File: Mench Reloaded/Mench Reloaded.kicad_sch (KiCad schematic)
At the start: 41 parts, among them IC1 DS1813, J2 Barrel_Jack_Switch, SW1 SW_Push, U1 W65C265SxQ, U5 LM7805_TO220, Y1 32.768 kHz, Y2 3.6864 mHz

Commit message: First draft of PCB
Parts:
- removed C10: 0.1uF, symbol Device:C_Small
- removed C11: 10uF, symbol Device:C_Polarized_US
- removed C9: 0.33uF, symbol Device:C_Small
- removed D1: LED, symbol Device:LED
- removed J2: Barrel_Jack_Switch, symbol Connector:Barrel_Jack_Switch
- removed R1: R_US, symbol Device:R_US
- removed U5: LM7805_TO220, Package_TO_SOT_THT:TO-220-3_Vertical, symbol Regulator_Linear:LM7805_TO220
- C1: renamed from C6; footprint (none) -> Capacitor_SMD:C_0805_2012Metric_Pad1.18x1.45mm_HandSolder
- C2: renamed from C8; footprint (none) -> Capacitor_SMD:C_0805_2012Metric_Pad1.18x1.45mm_HandSolder
- C3: renamed from C5; footprint (none) -> Capacitor_SMD:C_0805_2012Metric_Pad1.18x1.45mm_HandSolder
- C4: renamed from C7; footprint (none) -> Capacitor_SMD:C_0805_2012Metric_Pad1.18x1.45mm_HandSolder
- C5: renamed from C1; footprint (none) -> Capacitor_SMD:C_0805_2012Metric_Pad1.18x1.45mm_HandSolder
- C6: renamed from C2; footprint (none) -> Capacitor_SMD:C_0805_2012Metric_Pad1.18x1.45mm_HandSolder
- C7: renamed from C3; footprint (none) -> Capacitor_SMD:C_0805_2012Metric_Pad1.18x1.45mm_HandSolder
- C8: renamed from C4; footprint (none) -> Capacitor_SMD:C_0805_2012Metric_Pad1.18x1.45mm_HandSolder
- D1, D2, D3, D4, D5, D6, D7, D8: footprint (none) -> LED_SMD:LED_0805_2012Metric_Pad1.15x1.40mm_HandSolder
- IC1: footprint ds1813_revised-TO-92 -> ds1813_revised:ds1813_revised-TO-92
- R1: renamed from R4; footprint (none) -> Resistor_SMD:R_0805_2012Metric_Pad1.20x1.40mm_HandSolder
- R10: renamed from R11; footprint (none) -> Resistor_SMD:R_0805_2012Metric_Pad1.20x1.40mm_HandSolder
- R11: renamed from R12; footprint (none) -> Resistor_SMD:R_0805_2012Metric_Pad1.20x1.40mm_HandSolder
- R12: renamed from R13; footprint (none) -> Resistor_SMD:R_0805_2012Metric_Pad1.20x1.40mm_HandSolder
- R2: footprint (none) -> Resistor_SMD:R_0805_2012Metric_Pad1.20x1.40mm_HandSolder
- R3: renamed from R5; footprint (none) -> Resistor_SMD:R_0805_2012Metric_Pad1.20x1.40mm_HandSolder
- R4: renamed from R3; footprint (none) -> Resistor_SMD:R_0805_2012Metric_Pad1.20x1.40mm_HandSolder
- R5: renamed from R6; footprint (none) -> Resistor_SMD:R_0805_2012Metric_Pad1.20x1.40mm_HandSolder
- R6: renamed from R7; footprint (none) -> Resistor_SMD:R_0805_2012Metric_Pad1.20x1.40mm_HandSolder
- R7: renamed from R8; footprint (none) -> Resistor_SMD:R_0805_2012Metric_Pad1.20x1.40mm_HandSolder
- R8: renamed from R9; footprint (none) -> Resistor_SMD:R_0805_2012Metric_Pad1.20x1.40mm_HandSolder
- R9: renamed from R10; footprint (none) -> Resistor_SMD:R_0805_2012Metric_Pad1.20x1.40mm_HandSolder
- SW1: footprint (none) -> Button_Switch_THT:SW_PUSH_6mm_H5mm
- Y1: footprint (none) -> Crystal:Crystal_C26-LF_D2.1mm_L6.5mm_Horizontal
- Y2: footprint (none) -> Crystal:Crystal_HC49-U_Vertical
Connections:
- net BA: now reaches U1.39 (BA/~{DOD})
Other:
- moved on the sheet: C5, C6, C7, C8, D1, D2, D3, D4, D5, D6, D7, D8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

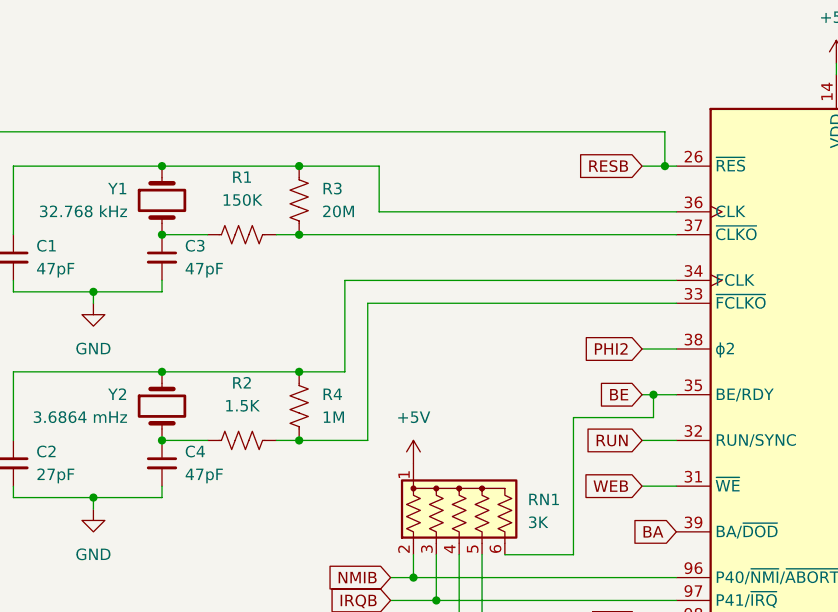
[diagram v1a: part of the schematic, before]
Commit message: Completed initial PCB layout. Commiting because I will try to reduce it to 100mm x 100mm
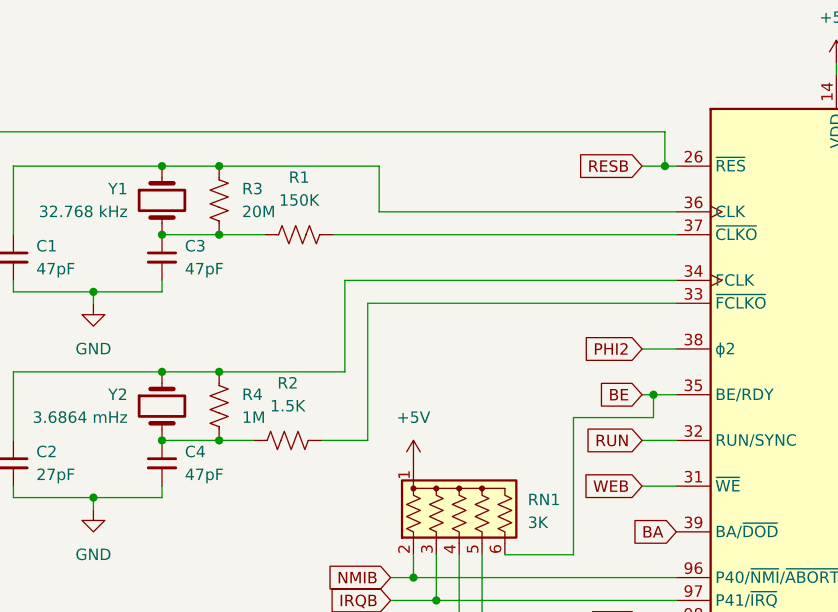
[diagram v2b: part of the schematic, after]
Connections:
- net at R2.2, U1.33 (~{FCLKO}): no longer R4.1
- net at R1.2, U1.37 (~{CLKO}): no longer R3.1
- net at C3.1, R1.1, Y1.2: now also R3.1
- net at C4.1, R2.1, Y2.2: now also R4.1
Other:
- moved on the sheet: R1, R2

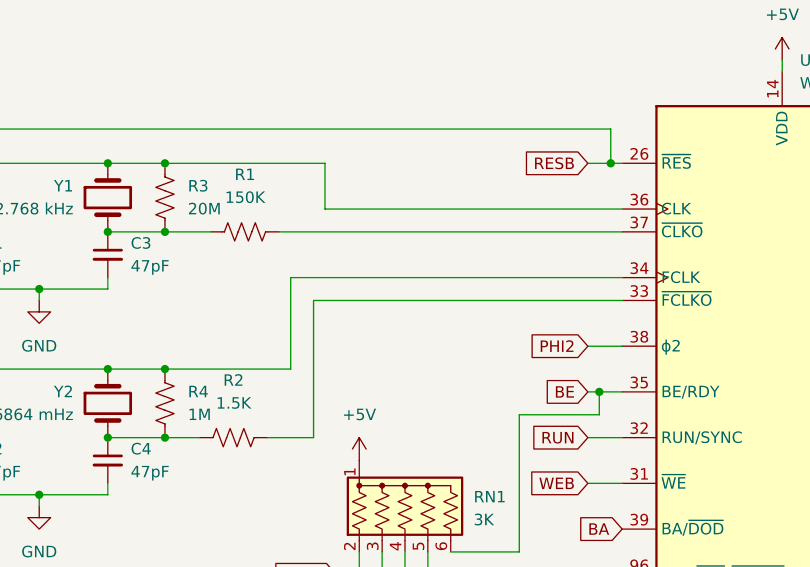
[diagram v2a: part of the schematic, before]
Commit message: Reworked the layout to 100mm by 100mm. Also changed the headers to be compatible with the W65C265SXB.
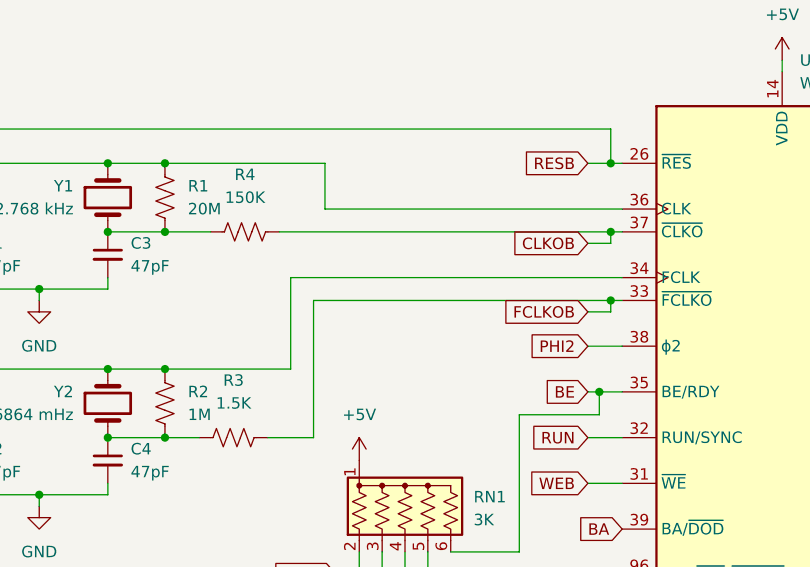
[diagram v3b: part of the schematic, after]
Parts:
- renumbered R3 to R1, R4 to R2, R2 to R3, R1 to R4
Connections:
- net FCLKOB: now reaches R3.2, U1.33 (~{FCLKO})
- net CLKOB: now reaches R4.2, U1.37 (~{CLKO})
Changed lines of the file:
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@@
   (junction (at 80.01 60.96) (diameter 0) (color 0 0 0 0)
   )
+  (junction (at 129.54 38.1) (diameter 0) (color 0 0 0 0)
+  )
   (junction (at 271.78 107.95) (diameter 0) (color 0 0 0 0)
   )
@@
   (junction (at 109.22 86.36) (diameter 0) (color 0 0 0 0)
   )
+  (junction (at 129.54 45.72) (diameter 0) (color 0 0 0 0)
+  )
   (junction (at 254 31.75) (diameter 0) (color 0 0 0 0)
   )
@@
     (stroke (width 0) (type default))
   )
-  (wire (pts (xy 96.52 45.72) (xy 130.81 45.72))
+  (wire (pts (xy 96.52 45.72) (xy 129.54 45.72))
     (stroke (width 0) (type default))
   )
@@
     (stroke (width 0) (type default))
   )
+  (wire (pts (xy 129.54 45.72) (xy 130.81 45.72))
+    (stroke (width 0) (type default))
+  )
   (bus (pts (xy 185.42 76.2) (xy 185.42 73.66))
     (stroke (width 0) (type default))
@@
     (stroke (width 0) (type default))
   )
+  (wire (pts (xy 129.54 38.1) (xy 129.54 39.37))
+    (stroke (width 0) (type default))
+  )
   (bus (pts (xy 185.42 121.92) (xy 185.42 119.38))
     (stroke (width 0) (type default))
@@
     (stroke (width 0) (type default))
   )
+  (wire (pts (xy 129.54 38.1) (xy 130.81 38.1))
+    (stroke (width 0) (type default))
+  )
   (wire (pts (xy 129.54 30.48) (xy 130.81 30.48))
     (stroke (width 0) (type default))
@@
     (stroke (width 0) (type default))
   )
+  (wire (pts (xy 127 46.99) (xy 129.54 46.99))
+    (stroke (width 0) (type default))
+  )
   (wire (pts (xy 129.54 26.67) (xy 44.45 26.67))
     (stroke (width 0) (type default))
@@
     (stroke (width 0) (type default))
   )
-  (wire (pts (xy 92.71 38.1) (xy 130.81 38.1))
+  (wire (pts (xy 92.71 38.1) (xy 129.54 38.1))
     (stroke (width 0) (type default))
   )
@@
     (stroke (width 0) (type default))
   )
+  (wire (pts (xy 129.54 46.99) (xy 129.54 45.72))
+    (stroke (width 0) (type default))
+  )
   (wire (pts (xy 271.78 87.63) (xy 271.78 97.79))
     (stroke (width 0) (type default))
@@
   )
   (wire (pts (xy 148.59 19.05) (xy 148.59 20.32))
+    (stroke (width 0) (type default))
+  )
+  (wire (pts (xy 129.54 39.37) (xy 127 39.37))
     (stroke (width 0) (type default))
   )
@@
     )
   )
+  (global_label "FCLKOB" (shape input) (at 127 46.99 180) (fields_autoplaced)
+    (effects (font (size 1.27 1.27)) (justify right))
+    (property "Intersheetrefs" "${INTERSHEET_REFS}" (at 116.7419 46.99 0)
+      (effects (font (size 1.27 1.27)) (justify right) hide)
+    )
+  )
   (global_label "csb[0..7]" (shape input) (at 242.57 83.82 180) (fields_autoplaced)
     (effects (font (size 1.27 1.27)) (justify right))
@@
     (effects (font (size 1.27 1.27)) (justify right))
     (property "Intersheetrefs" "${INTERSHEET_REFS}" (at 91.4629 83.82 0)
+      (effects (font (size 1.27 1.27)) (justify right) hide)
+    )
+  )
+  (global_label "CLKOB" (shape input) (at 127 39.37 180) (fields_autoplaced)
+    (effects (font (size 1.27 1.27)) (justify right))
+    (property "Intersheetrefs" "${INTERSHEET_REFS}" (at 117.8305 39.37 0)
       (effects (font (size 1.27 1.27)) (justify right) hide)
     )
@@
   (symbol (lib_id "Device:R_US") (at 80.01 34.29 180) (unit 1)
     (in_bom yes) (on_board yes) (dnp no) (fields_autoplaced)
-    (property "Reference" "R3" (at 82.55 33.02 0)
+    (property "Reference" "R1" (at 82.55 33.02 0)
       (effects (font (size 1.27 1.27)) (justify right))
     )
@@
       (project "Mench Reloaded"
         (path "/e63e39d7-6ac0-4ffd-8aa3-1841a4541b55"
-          (reference "R3") (unit 1)
+          (reference "R1") (unit 1)
         )
       )
@@
   (symbol (lib_id "Device:R_US") (at 88.9 38.1 90) (unit 1)
     (in_bom yes) (on_board yes) (dnp no) (fields_autoplaced)
-    (property "Reference" "R1" (at 88.9 31.75 90)
+    (property "Reference" "R4" (at 88.9 31.75 90)
       (effects (font (size 1.27 1.27)))
     )
@@
       (project "Mench Reloaded"
         (path "/e63e39d7-6ac0-4ffd-8aa3-1841a4541b55"
-          (reference "R1") (unit 1)
+          (reference "R4") (unit 1)
         )
       )
@@
   (symbol (lib_id "Device:R_US") (at 87.63 60.96 90) (unit 1)
     (in_bom yes) (on_board yes) (dnp no) (fields_autoplaced)
-    (property "Reference" "R2" (at 87.63 54.61 90)
+    (property "Reference" "R3" (at 87.63 54.61 90)
       (effects (font (size 1.27 1.27)))
     )
@@
       (project "Mench Reloaded"
         (path "/e63e39d7-6ac0-4ffd-8aa3-1841a4541b55"
-          (reference "R2") (unit 1)
+          (reference "R3") (unit 1)
         )
       )
@@
   (symbol (lib_id "Device:R_US") (at 80.01 57.15 180) (unit 1)
     (in_bom yes) (on_board yes) (dnp no) (fields_autoplaced)
-    (property "Reference" "R4" (at 82.55 55.88 0)
+    (property "Reference" "R2" (at 82.55 55.88 0)
       (effects (font (size 1.27 1.27)) (justify right))
     )
@@
       (project "Mench Reloaded"
         (path "/e63e39d7-6ac0-4ffd-8aa3-1841a4541b55"
-          (reference "R4") (unit 1)
-        )
-      )
+          (reference "R2") (unit 1)
+        )
+      )

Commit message: Increased the vertical spacing of the components. Aligned the 0-volt pins of the RAM and ROM. Made sure that no resistors or diodes are in the parallel feed area. Removed the unused chip select indicator diodes. I can add them to any cards that use the expansion header. Moved the interrupt select header and diode above the 65c22 because that area was available. For the 65c22 chip I used a5b for cs1 and cs1b for cs2b. This should map it to 0xDFC0.
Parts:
- removed D1, D3, D4, D6, D7, D8: green, LED_SMD:LED_0805_2012Metric_Pad1.15x1.40mm_HandSolder, symbol Device:LED_Small
- removed R10, R11, R12, R5, R7, R8: 3K, Resistor_SMD:R_0805_2012Metric_Pad1.20x1.40mm_HandSolder, symbol Device:R_US
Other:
- added sheet 65c22 IO (65c22 IO.kicad_sch)
- moved on the sheet: D2, D5, R6, R9

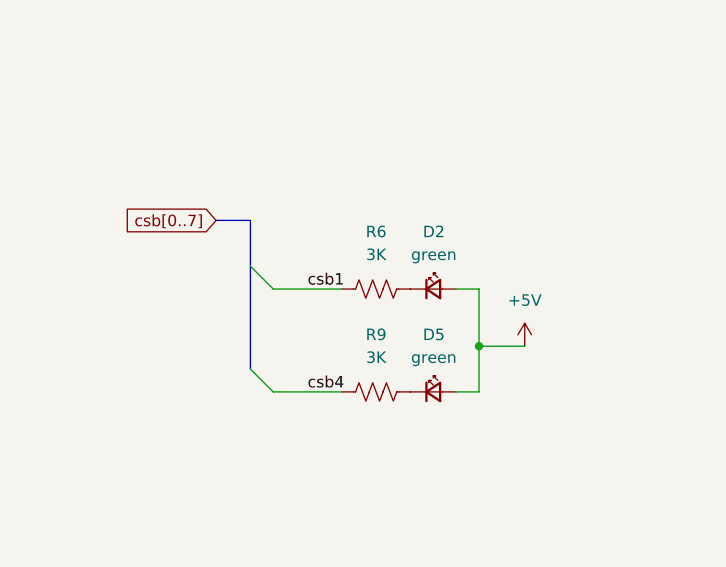
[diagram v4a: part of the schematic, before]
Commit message: Reworked the schematic to aid with routing. Began routing the pcb.
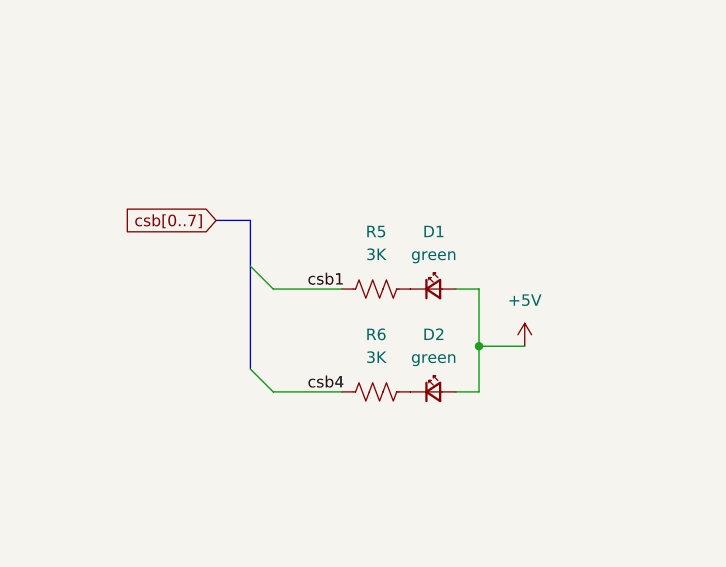
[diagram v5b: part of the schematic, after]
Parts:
- U1: footprint Package_QFP:PQFP-100_14x20mm_P0.65mm -> Mench Reloaded_footprints:PQFP-100_14x20mm_P0.65mm_HandSolder
- renumbered D2 to D1, D5 to D2, R6 to R5, R9 to R6
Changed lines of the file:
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@@
   (symbol (lib_id "Device:LED_Small") (at 266.7 91.44 0) (unit 1)
     (in_bom yes) (on_board yes) (dnp no)
-    (property "Reference" "D2" (at 266.7635 85.09 0)
+    (property "Reference" "D1" (at 266.7635 85.09 0)
       (effects (font (size 1.27 1.27)))
     )
@@
       (project "Mench Reloaded"
         (path "/e63e39d7-6ac0-4ffd-8aa3-1841a4541b55"
-          (reference "D2") (unit 1)
+          (reference "D1") (unit 1)
         )
       )
@@
       (effects (font (size 1.27 1.27)) (justify left))
     )
-    (property "Footprint" "Package_QFP:PQFP-100_14x20mm_P0.65mm" (at 148.59 7.62 0)
+    (property "Footprint" "Mench Reloaded_footprints:PQFP-100_14x20mm_P0.65mm_HandSolder" (at 148.59 7.62 0)
       (effects (font (size 1.27 1.27)) hide)
     )
@@
   (symbol (lib_id "Device:R_US") (at 260.35 91.44 90) (unit 1)
     (in_bom yes) (on_board yes) (dnp no) (fields_autoplaced)
-    (property "Reference" "R6" (at 260.35 85.09 90)
+    (property "Reference" "R5" (at 260.35 85.09 90)
       (effects (font (size 1.27 1.27)))
     )
@@
       (project "Mench Reloaded"
         (path "/e63e39d7-6ac0-4ffd-8aa3-1841a4541b55"
+          (reference "R5") (unit 1)
+        )
+      )
+    )
+  )
+  (symbol (lib_id "Device:R_US") (at 260.35 102.87 90) (unit 1)
+    (in_bom yes) (on_board yes) (dnp no) (fields_autoplaced)
+    (property "Reference" "R6" (at 260.35 96.52 90)
+      (effects (font (size 1.27 1.27)))
+    )
+    (property "Value" "3K" (at 260.35 99.06 90)
+      (effects (font (size 1.27 1.27)))
+    )
+    (property "Footprint" "Resistor_SMD:R_0805_2012Metric_Pad1.20x1.40mm_HandSolder" (at 260.604 101.854 90)
+      (effects (font (size 1.27 1.27)) hide)
+    )
+    (property "Datasheet" "~" (at 260.35 102.87 0)
+      (effects (font (size 1.27 1.27)) hide)
+    )
+    (pin "1")
+    (pin "2")
+    (instances
+      (project "Mench Reloaded"
+        (path "/e63e39d7-6ac0-4ffd-8aa3-1841a4541b55"
           (reference "R6") (unit 1)
-        )
-      )
-    )
-  )
-  (symbol (lib_id "Device:R_US") (at 260.35 102.87 90) (unit 1)
-    (in_bom yes) (on_board yes) (dnp no) (fields_autoplaced)
-    (property "Reference" "R9" (at 260.35 96.52 90)
-      (effects (font (size 1.27 1.27)))
-    )
-    (property "Value" "3K" (at 260.35 99.06 90)
-      (effects (font (size 1.27 1.27)))
-    )
-    (property "Footprint" "Resistor_SMD:R_0805_2012Metric_Pad1.20x1.40mm_HandSolder" (at 260.604 101.854 90)
-      (effects (font (size 1.27 1.27)) hide)
-    )
-    (property "Datasheet" "~" (at 260.35 102.87 0)
-      (effects (font (size 1.27 1.27)) hide)
-    )
-    (pin "1")
-    (pin "2")
-    (instances
-      (project "Mench Reloaded"
-        (path "/e63e39d7-6ac0-4ffd-8aa3-1841a4541b55"
-          (reference "R9") (unit 1)
         )
       )
@@
   (symbol (lib_id "Device:LED_Small") (at 266.7 102.87 0) (unit 1)
     (in_bom yes) (on_board yes) (dnp no)
-    (property "Reference" "D5" (at 266.7635 96.52 0)
+    (property "Reference" "D2" (at 266.7635 96.52 0)
       (effects (font (size 1.27 1.27)))
     )
@@
       (project "Mench Reloaded"
         (path "/e63e39d7-6ac0-4ffd-8aa3-1841a4541b55"
-          (reference "D5") (unit 1)
-        )
-      )
+          (reference "D2") (unit 1)
+        )
+      )

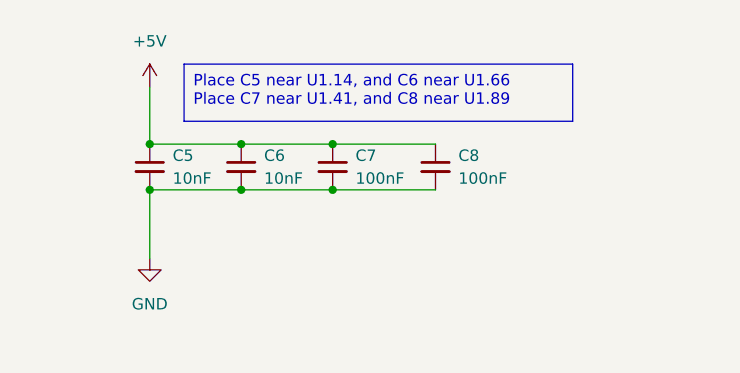
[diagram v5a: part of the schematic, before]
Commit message: Completed all traces. Added a Zif socket footprint to ensure one will fit. Added a solder jumper for RAM options.
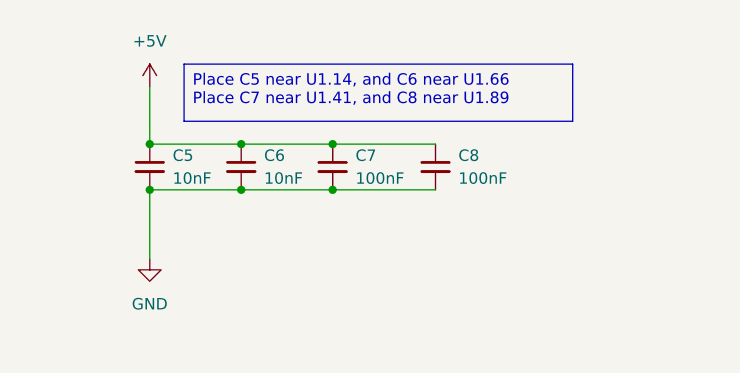
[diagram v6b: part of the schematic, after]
